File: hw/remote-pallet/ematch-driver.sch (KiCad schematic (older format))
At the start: 7 parts, among them Q2 Q_PMOS_DGS, Q3 Q_NMOS_DGS

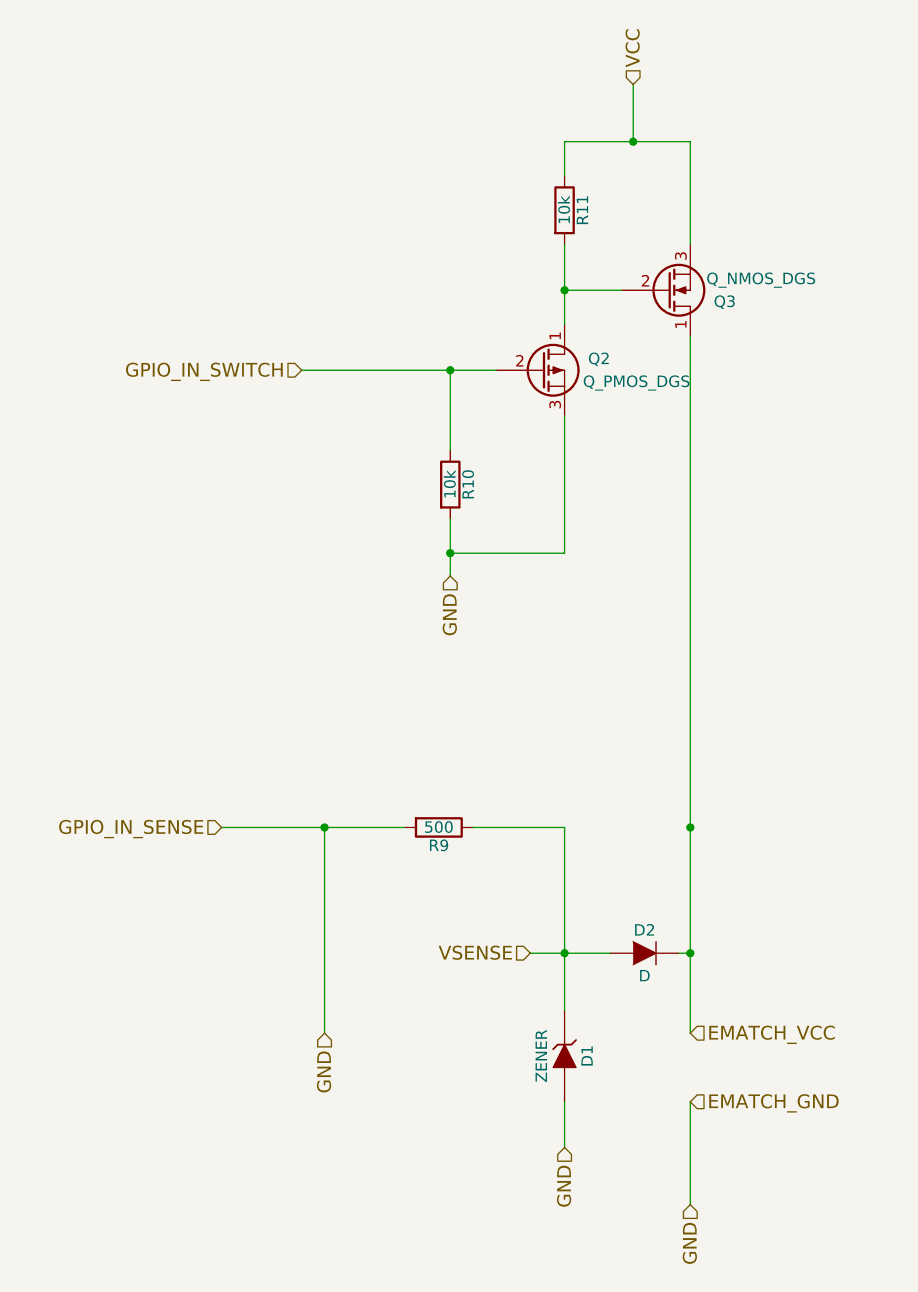
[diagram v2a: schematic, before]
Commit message: updating schematic and starting board layout
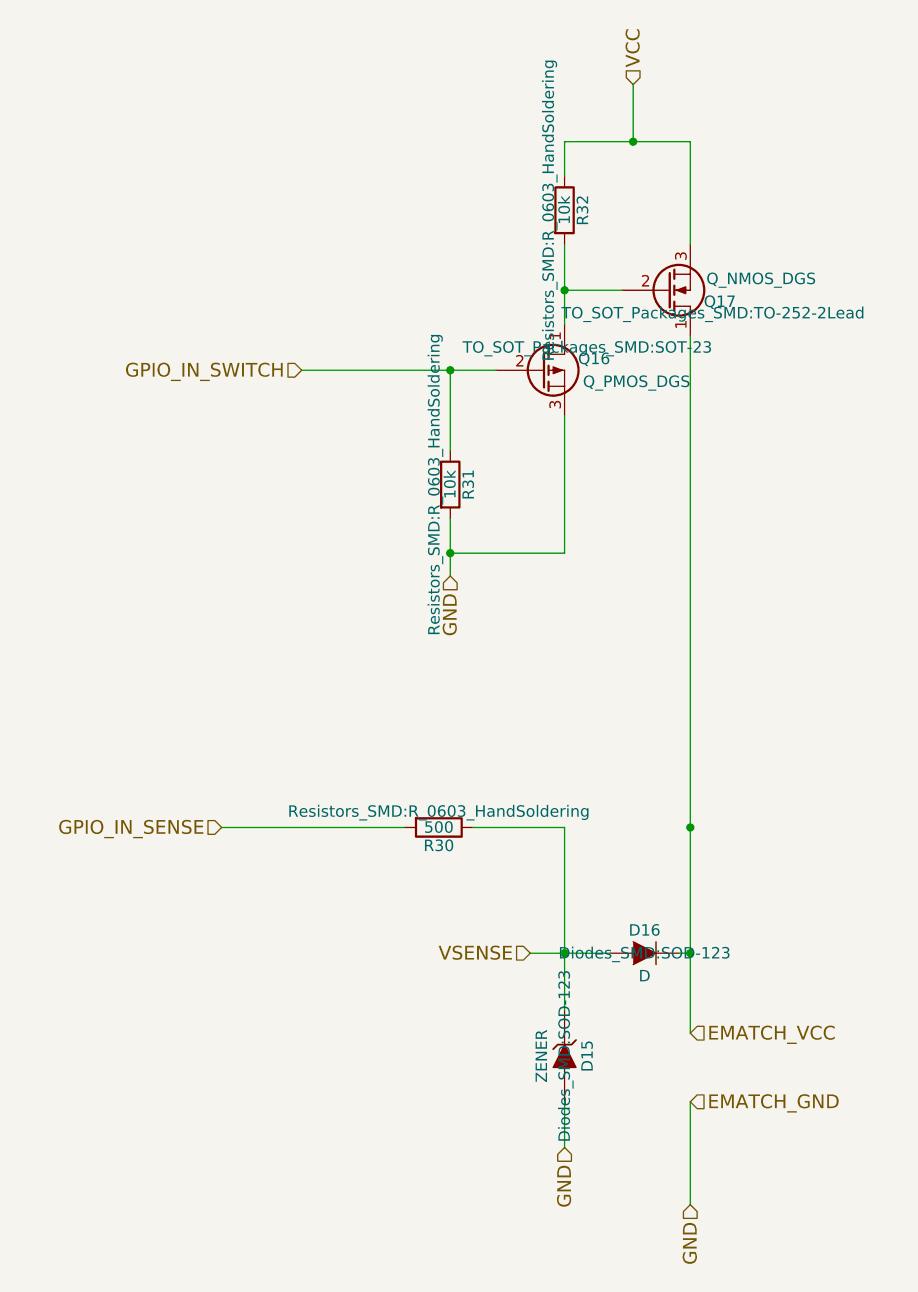
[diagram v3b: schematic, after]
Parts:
- D1, D2: footprint (none) -> Diodes_SMD:SOD-123
- Q2: footprint (none) -> TO_SOT_Packages_SMD:SOT-23
- Q3: footprint (none) -> TO_SOT_Packages_SMD:TO-252-2Lead
- R10, R11, R9: footprint (none) -> Resistors_SMD:R_0603_HandSoldering
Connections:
- net EMATCH_GND: no longer R9.2
- new net GPIO_IN_SENSE: R9.2
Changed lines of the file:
@@
 LIBS:valves
 LIBS:iot_photon_headers
+LIBS:particle-boards
 LIBS:remote-pallet-cache
 EELAYER 25 0
@@
 AR Path="/56EAA68A/56CFCF8E" Ref="R27"  Part="1"
 AR Path="/56EAA6CF/56CFCF8E" Ref="R30"  Part="1"
-F 0 "R9" V 3080 4100 50  0000 C CNN
+F 0 "R30" V 3080 4100 50  0000 C CNN
 F 1 "500" V 3000 4100 50  0000 C CNN
-F 2 "" V 2930 4100 50  0000 C CNN
+F 2 "Resistors_SMD:R_0603_HandSoldering" V 2930 4100 50  0000 C CNN
 F 3 "" H 3000 4100 50  0000 C CNN
 	1    3000 4100
@@
 AR Path="/56EAA68A/56CFD0B3" Ref="R28"  Part="1"
 AR Path="/56EAA6CF/56CFD0B3" Ref="R31"  Part="1"
-F 0 "R10" V 3130 2600 50  0000 C CNN
+F 0 "R31" V 3130 2600 50  0000 C CNN
 F 1 "10k" V 3050 2600 50  0000 C CNN
-F 2 "" V 2980 2600 50  0000 C CNN
+F 2 "Resistors_SMD:R_0603_HandSoldering" V 2980 2600 50  0000 C CNN
 F 3 "" H 3050 2600 50  0000 C CNN
 	1    3050 2600
@@
 AR Path="/56EAA68A/56CFD248" Ref="Q15"  Part="1"
 AR Path="/56EAA6CF/56CFD248" Ref="Q17"  Part="1"
-F 0 "Q3" H 4300 1800 50  0000 R CNN
+F 0 "Q17" H 4300 1800 50  0000 R CNN
 F 1 "Q_NMOS_DGS" H 4650 1700 50  0000 R CNN
-F 2 "" H 4200 1850 50  0000 C CNN
+F 2 "TO_SOT_Packages_SMD:TO-252-2Lead" H 4200 1850 50  0000 C CNN
 F 3 "" H 4000 1750 50  0000 C CNN
 	1    4000 1750
@@
 AR Path="/56EAA68A/56CFDBA4" Ref="Q14"  Part="1"
 AR Path="/56EAA6CF/56CFDBA4" Ref="Q16"  Part="1"
-F 0 "Q2" H 3750 2150 50  0000 R CNN
+F 0 "Q16" H 3750 2150 50  0000 R CNN
 F 1 "Q_PMOS_DGS" H 4100 2050 50  0000 R CNN
-F 2 "" H 3650 2200 50  0000 C CNN
+F 2 "TO_SOT_Packages_SMD:SOT-23" H 3650 2200 50  0000 C CNN
 F 3 "" H 3450 2100 50  0000 C CNN
 	1    3450 2100
@@
 AR Path="/56EAA68A/56CFDBE5" Ref="R29"  Part="1"
 AR Path="/56EAA6CF/56CFDBE5" Ref="R32"  Part="1"
-F 0 "R11" V 3630 1400 50  0000 C CNN
+F 0 "R32" V 3630 1400 50  0000 C CNN
 F 1 "10k" V 3550 1400 50  0000 C CNN
-F 2 "" V 3480 1400 50  0000 C CNN
+F 2 "Resistors_SMD:R_0603_HandSoldering" V 3480 1400 50  0000 C CNN
 F 3 "" H 3550 1400 50  0000 C CNN
 	1    3550 1400
@@
 AR Path="/56EAA68A/56CFDC9F" Ref="D14"  Part="1"
 AR Path="/56EAA6CF/56CFDC9F" Ref="D16"  Part="1"
-F 0 "D2" H 3900 4750 50  0000 C CNN
+F 0 "D16" H 3900 4750 50  0000 C CNN
 F 1 "D" H 3900 4550 50  0000 C CNN
-F 2 "" H 3900 4650 50  0000 C CNN
+F 2 "Diodes_SMD:SOD-123" H 3900 4650 50  0000 C CNN
 F 3 "" H 3900 4650 50  0000 C CNN
 	1    3900 4650
@@
 AR Path="/56EAA68A/56CFDD3A" Ref="D13"  Part="1"
 AR Path="/56EAA6CF/56CFDD3A" Ref="D15"  Part="1"
-F 0 "D1" H 3550 5200 50  0000 C CNN
+F 0 "D15" H 3550 5200 50  0000 C CNN
 F 1 "ZENER" H 3550 5000 50  0000 C CNN
-F 2 "" H 3550 5100 50  0000 C CNN
+F 2 "Diodes_SMD:SOD-123" H 3550 5100 50  0000 C CNN
 F 3 "" H 3550 5100 50  0000 C CNN
 	1    3550 5100
@@
 	4100 1950 4100 5000
 Wire Wire Line
-	2500 4100 2500 5000
-Wire Wire Line
 	2050 4100 2850 4100
 Wire Wire Line
@@
 Wire Wire Line
 	4100 5300 4100 5750
-Connection ~ 2500 4100
 Wire Wire Line
 	3550 4100 3550 4900
@@
 Text HLabel 3050 3000 3    60   Input ~ 0
 GND
-Text HLabel 2500 5000 3    60   Input ~ 0
-GND
 Text HLabel 3550 5500 3    60   Input ~ 0

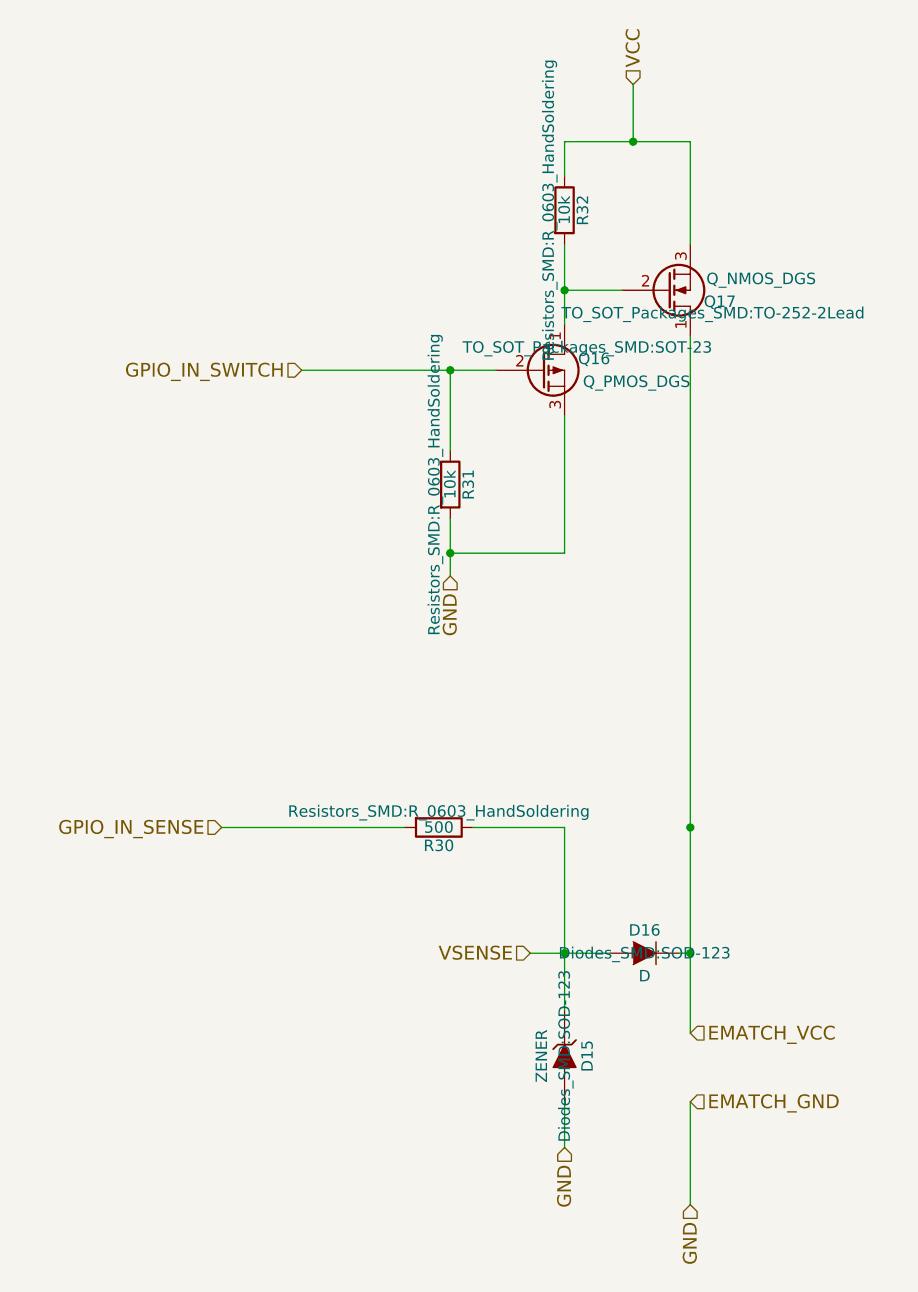
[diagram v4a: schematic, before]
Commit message: adding some new footprints, laying out board
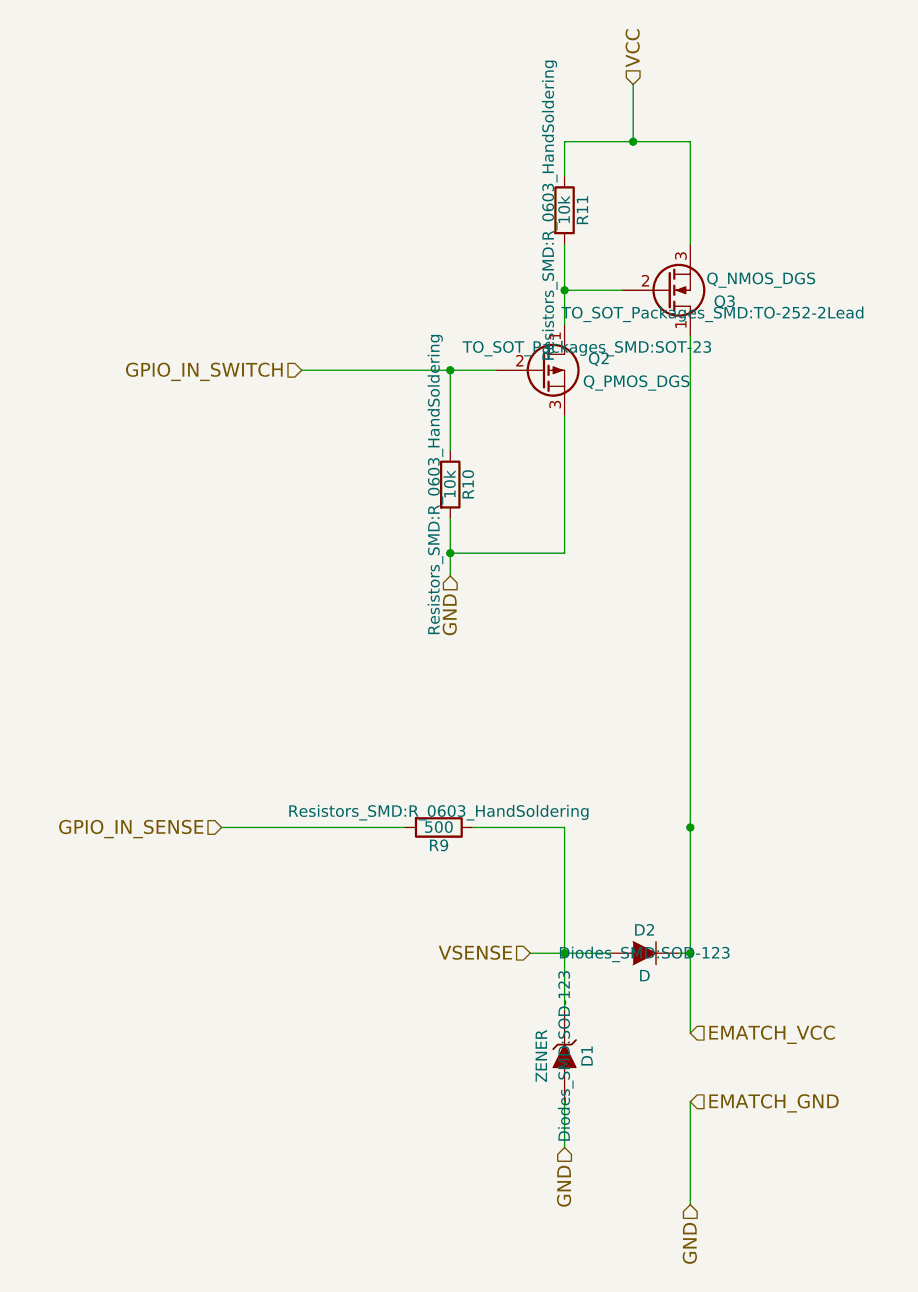
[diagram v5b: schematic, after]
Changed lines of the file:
@@
 LIBS:valves
 LIBS:particle-boards
+LIBS:IC REG LDO 3.3V 0.2A SOT23-5
 LIBS:remote-pallet-cache
 EELAYER 25 0
@@
 AR Path="/56EAA68A/56CFCF8E" Ref="R27"  Part="1"
 AR Path="/56EAA6CF/56CFCF8E" Ref="R30"  Part="1"
-F 0 "R30" V 3080 4100 50  0000 C CNN
+F 0 "R9" V 3080 4100 50  0000 C CNN
 F 1 "500" V 3000 4100 50  0000 C CNN
 F 2 "Resistors_SMD:R_0603_HandSoldering" V 2930 4100 50  0000 C CNN
@@
 AR Path="/56EAA68A/56CFD0B3" Ref="R28"  Part="1"
 AR Path="/56EAA6CF/56CFD0B3" Ref="R31"  Part="1"
-F 0 "R31" V 3130 2600 50  0000 C CNN
+F 0 "R10" V 3130 2600 50  0000 C CNN
 F 1 "10k" V 3050 2600 50  0000 C CNN
 F 2 "Resistors_SMD:R_0603_HandSoldering" V 2980 2600 50  0000 C CNN
@@
 AR Path="/56EAA68A/56CFD248" Ref="Q15"  Part="1"
 AR Path="/56EAA6CF/56CFD248" Ref="Q17"  Part="1"
-F 0 "Q17" H 4300 1800 50  0000 R CNN
+F 0 "Q3" H 4300 1800 50  0000 R CNN
 F 1 "Q_NMOS_DGS" H 4650 1700 50  0000 R CNN
 F 2 "TO_SOT_Packages_SMD:TO-252-2Lead" H 4200 1850 50  0000 C CNN
@@
 AR Path="/56EAA68A/56CFDBA4" Ref="Q14"  Part="1"
 AR Path="/56EAA6CF/56CFDBA4" Ref="Q16"  Part="1"
-F 0 "Q16" H 3750 2150 50  0000 R CNN
+F 0 "Q2" H 3750 2150 50  0000 R CNN
 F 1 "Q_PMOS_DGS" H 4100 2050 50  0000 R CNN
 F 2 "TO_SOT_Packages_SMD:SOT-23" H 3650 2200 50  0000 C CNN
@@
 AR Path="/56EAA68A/56CFDBE5" Ref="R29"  Part="1"
 AR Path="/56EAA6CF/56CFDBE5" Ref="R32"  Part="1"
-F 0 "R32" V 3630 1400 50  0000 C CNN
+F 0 "R11" V 3630 1400 50  0000 C CNN
 F 1 "10k" V 3550 1400 50  0000 C CNN
 F 2 "Resistors_SMD:R_0603_HandSoldering" V 3480 1400 50  0000 C CNN
@@
 AR Path="/56EAA68A/56CFDC9F" Ref="D14"  Part="1"
 AR Path="/56EAA6CF/56CFDC9F" Ref="D16"  Part="1"
-F 0 "D16" H 3900 4750 50  0000 C CNN
+F 0 "D2" H 3900 4750 50  0000 C CNN
 F 1 "D" H 3900 4550 50  0000 C CNN
 F 2 "Diodes_SMD:SOD-123" H 3900 4650 50  0000 C CNN
@@
 AR Path="/56EAA68A/56CFDD3A" Ref="D13"  Part="1"
 AR Path="/56EAA6CF/56CFDD3A" Ref="D15"  Part="1"
-F 0 "D15" H 3550 5200 50  0000 C CNN
+F 0 "D1" H 3550 5200 50  0000 C CNN
 F 1 "ZENER" H 3550 5000 50  0000 C CNN
 F 2 "Diodes_SMD:SOD-123" H 3550 5100 50  0000 C CNN

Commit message: changes to layout adding debug LEDs
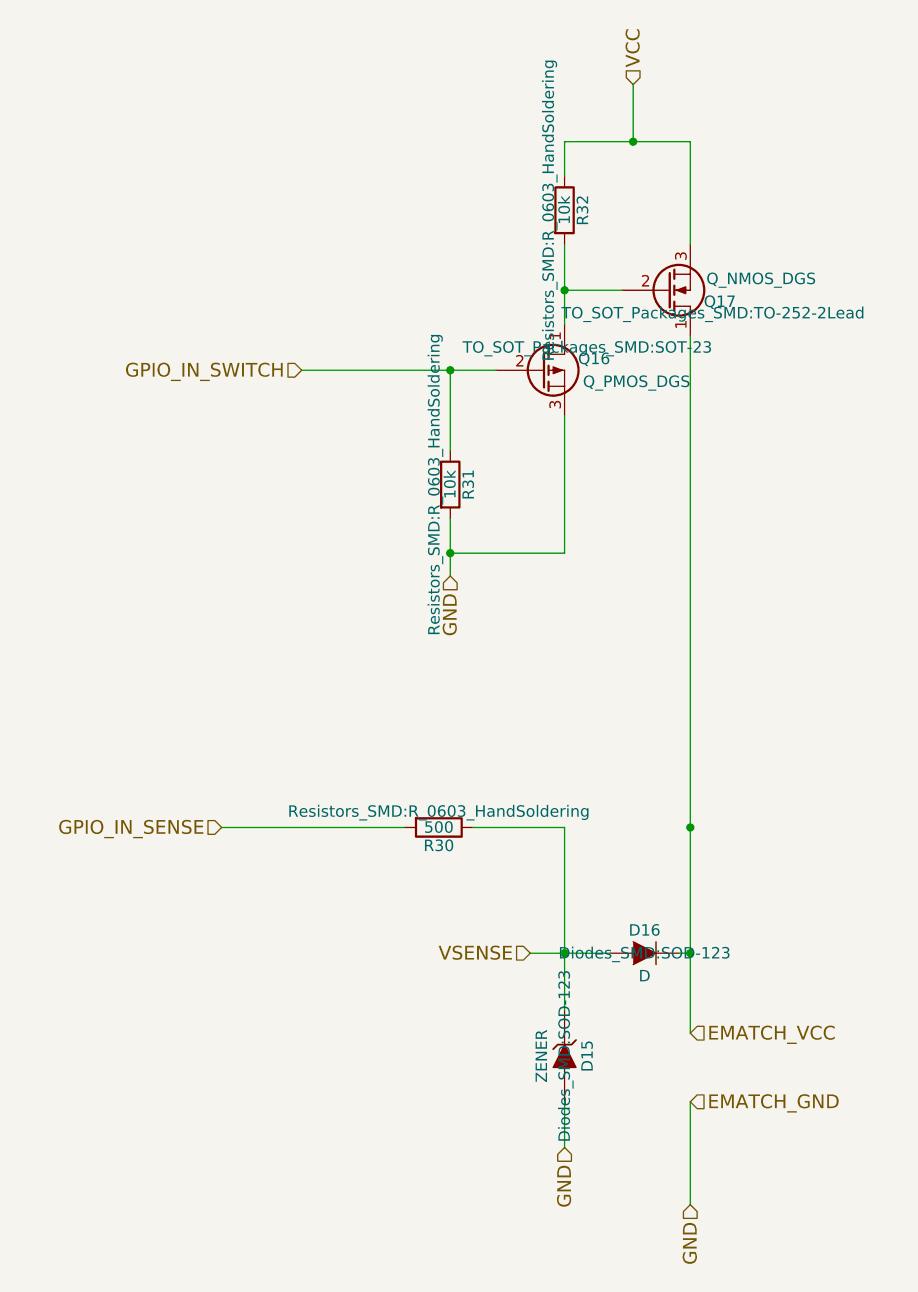
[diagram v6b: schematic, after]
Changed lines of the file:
@@
 AR Path="/56EAA68A/56CFCF8E" Ref="R27"  Part="1"
 AR Path="/56EAA6CF/56CFCF8E" Ref="R30"  Part="1"
-F 0 "R9" V 3080 4100 50  0000 C CNN
+F 0 "R30" V 3080 4100 50  0000 C CNN
 F 1 "500" V 3000 4100 50  0000 C CNN
 F 2 "Resistors_SMD:R_0603_HandSoldering" V 2930 4100 50  0000 C CNN
@@
 AR Path="/56EAA68A/56CFD0B3" Ref="R28"  Part="1"
 AR Path="/56EAA6CF/56CFD0B3" Ref="R31"  Part="1"
-F 0 "R10" V 3130 2600 50  0000 C CNN
+F 0 "R31" V 3130 2600 50  0000 C CNN
 F 1 "10k" V 3050 2600 50  0000 C CNN
 F 2 "Resistors_SMD:R_0603_HandSoldering" V 2980 2600 50  0000 C CNN
@@
 AR Path="/56EAA68A/56CFD248" Ref="Q15"  Part="1"
 AR Path="/56EAA6CF/56CFD248" Ref="Q17"  Part="1"
-F 0 "Q3" H 4300 1800 50  0000 R CNN
+F 0 "Q17" H 4300 1800 50  0000 R CNN
 F 1 "Q_NMOS_DGS" H 4650 1700 50  0000 R CNN
 F 2 "TO_SOT_Packages_SMD:TO-252-2Lead" H 4200 1850 50  0000 C CNN
@@
 AR Path="/56EAA68A/56CFDBA4" Ref="Q14"  Part="1"
 AR Path="/56EAA6CF/56CFDBA4" Ref="Q16"  Part="1"
-F 0 "Q2" H 3750 2150 50  0000 R CNN
+F 0 "Q16" H 3750 2150 50  0000 R CNN
 F 1 "Q_PMOS_DGS" H 4100 2050 50  0000 R CNN
 F 2 "TO_SOT_Packages_SMD:SOT-23" H 3650 2200 50  0000 C CNN
@@
 AR Path="/56EAA68A/56CFDBE5" Ref="R29"  Part="1"
 AR Path="/56EAA6CF/56CFDBE5" Ref="R32"  Part="1"
-F 0 "R11" V 3630 1400 50  0000 C CNN
+F 0 "R32" V 3630 1400 50  0000 C CNN
 F 1 "10k" V 3550 1400 50  0000 C CNN
 F 2 "Resistors_SMD:R_0603_HandSoldering" V 3480 1400 50  0000 C CNN
@@
 AR Path="/56EAA68A/56CFDC9F" Ref="D14"  Part="1"
 AR Path="/56EAA6CF/56CFDC9F" Ref="D16"  Part="1"
-F 0 "D2" H 3900 4750 50  0000 C CNN
+F 0 "D16" H 3900 4750 50  0000 C CNN
 F 1 "D" H 3900 4550 50  0000 C CNN
 F 2 "Diodes_SMD:SOD-123" H 3900 4650 50  0000 C CNN
@@
 AR Path="/56EAA68A/56CFDD3A" Ref="D13"  Part="1"
 AR Path="/56EAA6CF/56CFDD3A" Ref="D15"  Part="1"
-F 0 "D1" H 3550 5200 50  0000 C CNN
+F 0 "D15" H 3550 5200 50  0000 C CNN
 F 1 "ZENER" H 3550 5000 50  0000 C CNN
 F 2 "Diodes_SMD:SOD-123" H 3550 5100 50  0000 C CNN
